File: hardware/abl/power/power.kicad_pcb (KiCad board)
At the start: 2 copper layers, 110 x 80.4 mm, 41 parts, among them J1 Terminal_01x03, J2 Terminal_01x03, J3 009159008603906, U1 TWGMC AMS1117-3.3, U2 TMP1075D, U3 INA219AxD, U4 24AA025E48T-I/OT

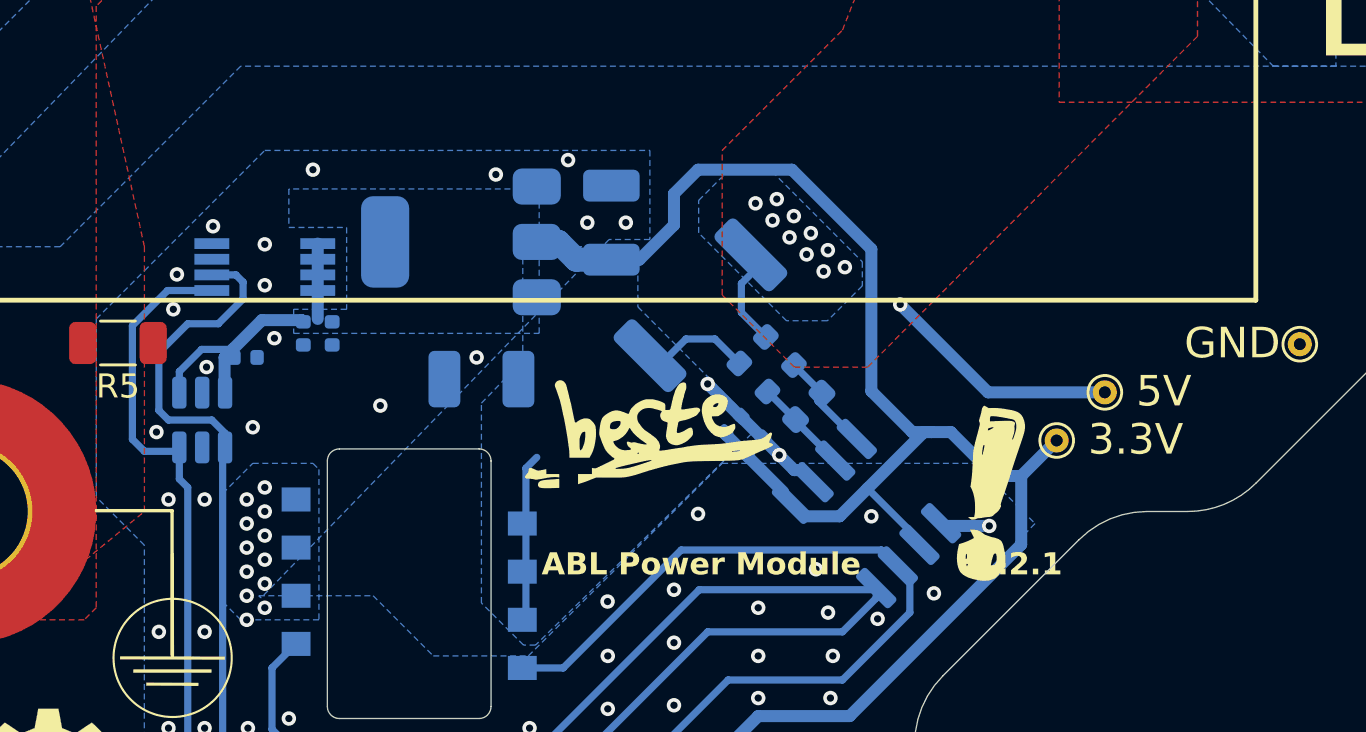
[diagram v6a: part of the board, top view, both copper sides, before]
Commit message: Move capacitor to avoid collision with power box enclosure.
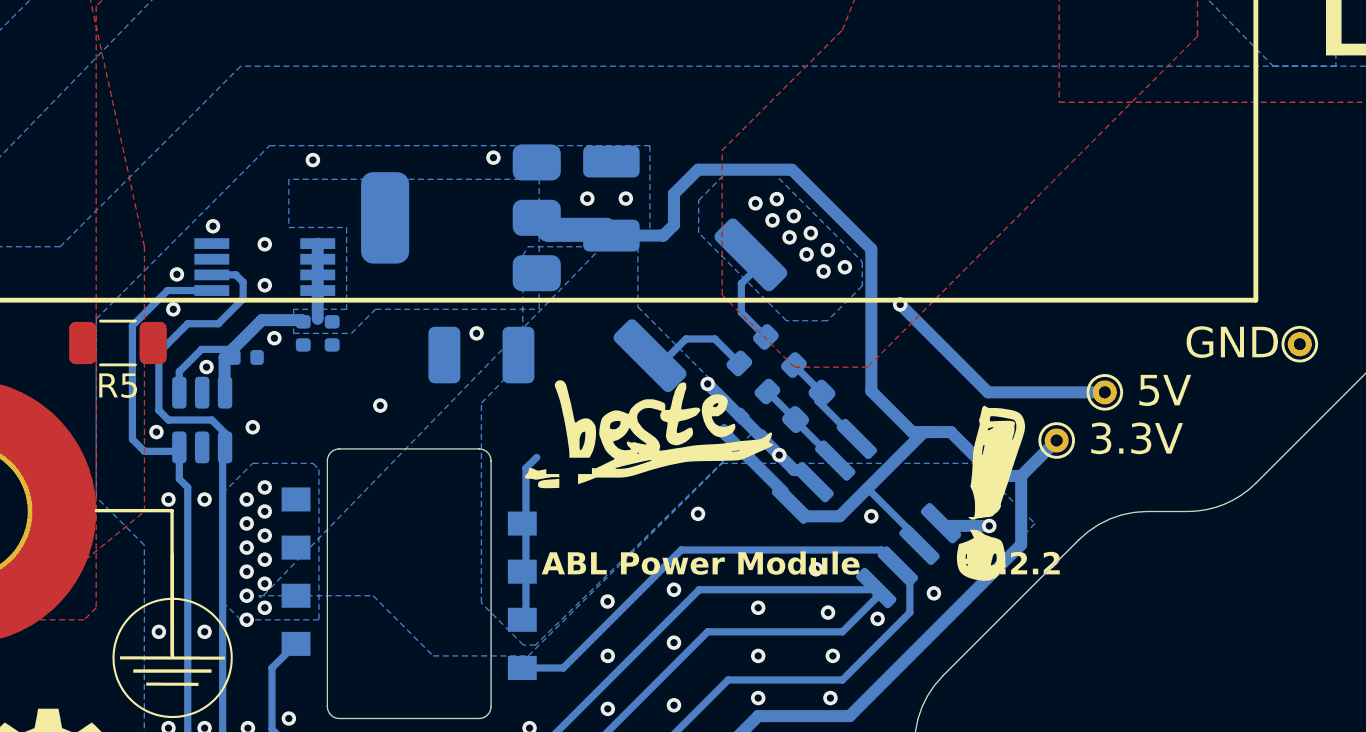
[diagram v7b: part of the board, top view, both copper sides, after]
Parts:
- moved C1 1.00 mm to (153.0, 90.5)
- moved C7 1.00 mm to (158.4, 84.0)
- moved U1 1.00 mm to (152.2, 84.8)
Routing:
- net GND: vias 70 -> 69
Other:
- board text added: "ABL Power Module v1.2.2"
- board text removed: "ABL Power Module v1.2.1"

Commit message: WIP feature conf (does not compile)
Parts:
- moved R5 0.90 mm to (137.0, 90.0)
- moved U4 0.90 mm to (140.5, 93.2)
- moved C8 0.50 mm to (143.2, 91.1)
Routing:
- net +3.3V: track 109.3 -> 105.9 mm
- net /SCL: track 89.9 -> 91.1 mm
- net GND: vias 69 -> 72
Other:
- board text added: "ABL Power Module v1.3"
- board text removed: "ABL Power Module v1.2.2"
